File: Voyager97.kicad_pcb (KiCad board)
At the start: 2 copper layers, 388.9 x 122.2 mm, 353 parts, among them J1 AVR-ISP-6, Q1 DSS60601MZ4-13, SW1 SW_Push, U1 AT90USB1286-AU, U2 PRTR5V0U2X, Y1 16MHz

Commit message: Generate production data
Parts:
- added G***: LOGO, locallib:ai-ring-6mm-FancyAss, B.Cu at (139.7, 136.5)
- added G***: LOGO, locallib:ai-ring-6mm-FancyAss-Mask, B.Cu at (139.7, 136.5)
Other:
- board text added: "Designed by ai03"

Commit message: Routing tweaks
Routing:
- net LEDGND: track 2355.3 -> 2356.9 mm
- net ROW3: track 473.7 -> 472.5 mm

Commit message: Add flex cut in center
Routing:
- net COL6: track 289.6 -> 483.0 mm
- net COL7: track 270.4 -> 447.7 mm
- net COL5: track 331.5 -> 488.2 mm
- net COL8: track 252.2 -> 392.7 mm
- net COL4: track 328.9 -> 448.7 mm
- net COL9: track 266.4 -> 370.1 mm
- net COL3: track 350.0 -> 428.4 mm, vias 0 -> 1
- net COL10: track 240.4 -> 304.7 mm, vias 0 -> 1
- net COL2: track 391.8 -> 433.4 mm, vias 0 -> 1
- net +5V: track 2867.6 -> 2836.5 mm, vias 7 -> 8
- net COL11: track 215.7 -> 244.2 mm, vias 0 -> 1
- net COL1: track 389.1 -> 395.3 mm
- net RESET: track 409.9 -> 408.0 mm
- net COL12: track 202.8 -> 203.8 mm
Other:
- outline, holes or cut-outs redrawn

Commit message: Add more flex cutouts
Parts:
- removed SW1: SW_Push, Molex-0548190589:PushButton_6x6mm_TH
- moved D52 20.6 mm to (56.4, 100.0)
- moved R52 20.6 mm to (56.4, 105.6)
- moved D47 15.9 mm to (271.5, 81.0)
- moved D63 15.9 mm to (257.2, 100.0)
- moved R47 15.9 mm to (271.5, 86.5)
- moved R63 15.9 mm to (257.2, 105.6)
- moved D77 15.9 mm to (247.7, 119.1)
- moved R77 15.9 mm to (247.7, 124.6)
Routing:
- net RESET: track 408.0 -> 46.1 mm, vias 3 -> 0
- net GND: track 546.9 -> 201.5 mm, vias 4 -> 3
- net ROW3: track 472.5 -> 455.6 mm
- net LEDGND: track 2356.9 -> 2346.1 mm
- net Net-(D63-Pad2): track 6.62 -> 16.2 mm, vias 0 -> 1
- net Net-(D47-Pad2): track 6.62 -> 12.7 mm
- net Net-(D77-Pad2): track 6.62 -> 12.7 mm
- net ROW4: track 424.0 -> 428.8 mm
- net ROW2: track 393.3 -> 398.1 mm
- net Net-(MX_'1-Pad4): track 7.18 -> 10.9 mm
- net COL11: track 244.2 -> 247.3 mm
- net Net-(MX_]1-Pad4): track 7.18 -> 10.0 mm
- net Net-(MX_/1-Pad4): track 7.18 -> 10.0 mm
- net Net-(CL1-1-Pad2): track 16.4 -> 18.5 mm
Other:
- outline, holes or cut-outs redrawn

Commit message: Adjust cutout location for durability
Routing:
- net LEDGND: track 2346.1 -> 2344.7 mm
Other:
- outline, holes or cut-outs redrawn

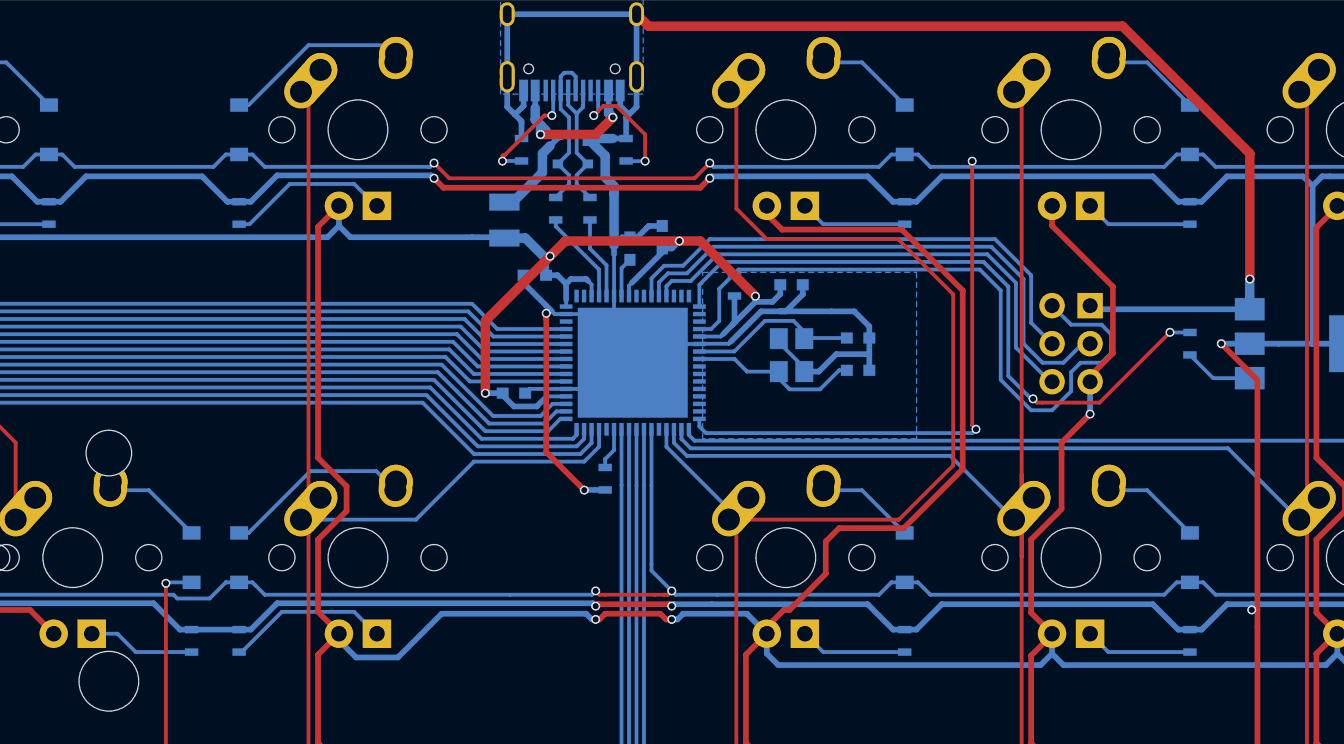
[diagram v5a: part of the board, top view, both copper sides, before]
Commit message: Optimizations
- Crystal placement
- Tracks near SPI header
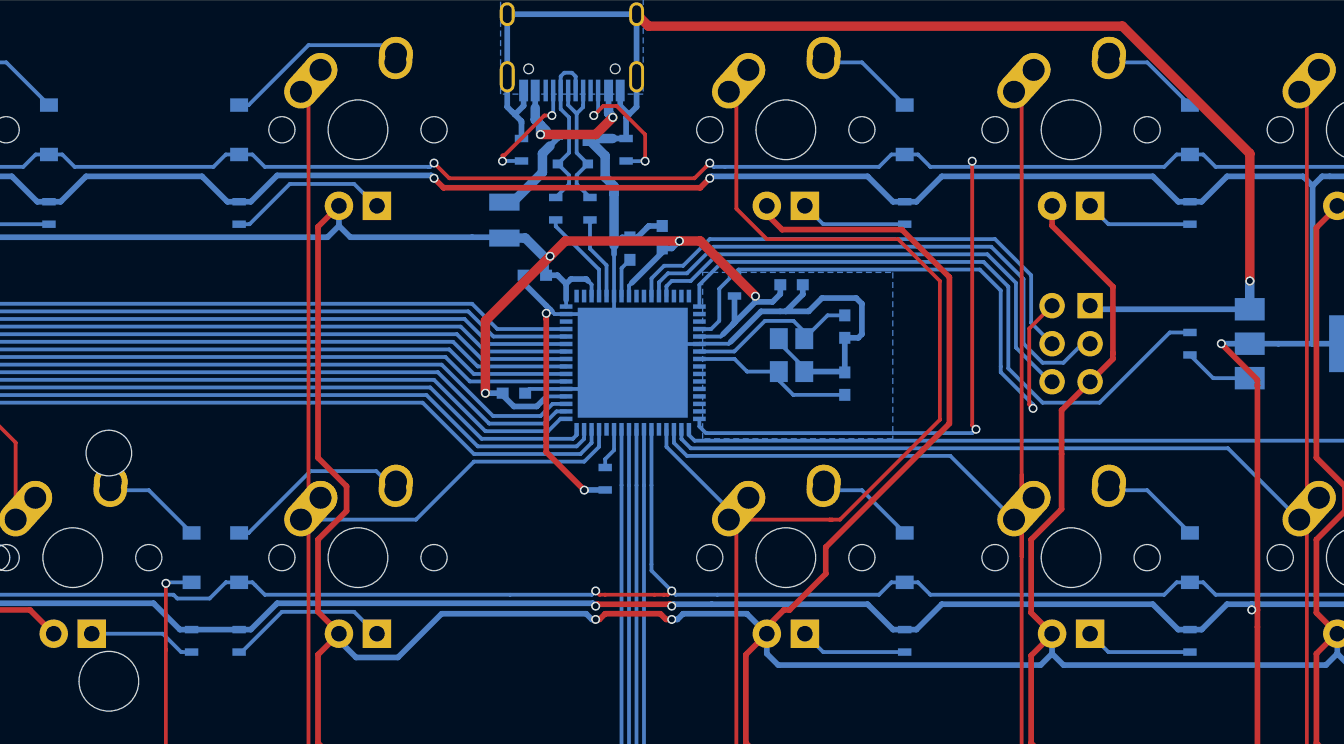
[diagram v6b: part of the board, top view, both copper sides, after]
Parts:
- moved C3 1.26 mm to (359.5, 50.3), turned to 90 degrees
- moved C4 1.17 mm to (359.5, 46.5), turned to 270 degrees
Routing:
- net RESET: track 46.1 -> 40.0 mm, vias 0 -> 1
- net +5V: track 2836.5 -> 2833.3 mm, vias 8 -> 7
- net COL15: track 149.9 -> 147.0 mm
- net Net-(RC5-Pad1): track 44.2 -> 43.9 mm, vias 2 -> 0
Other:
- net class Power: trace_width 0.381 -> 0.635

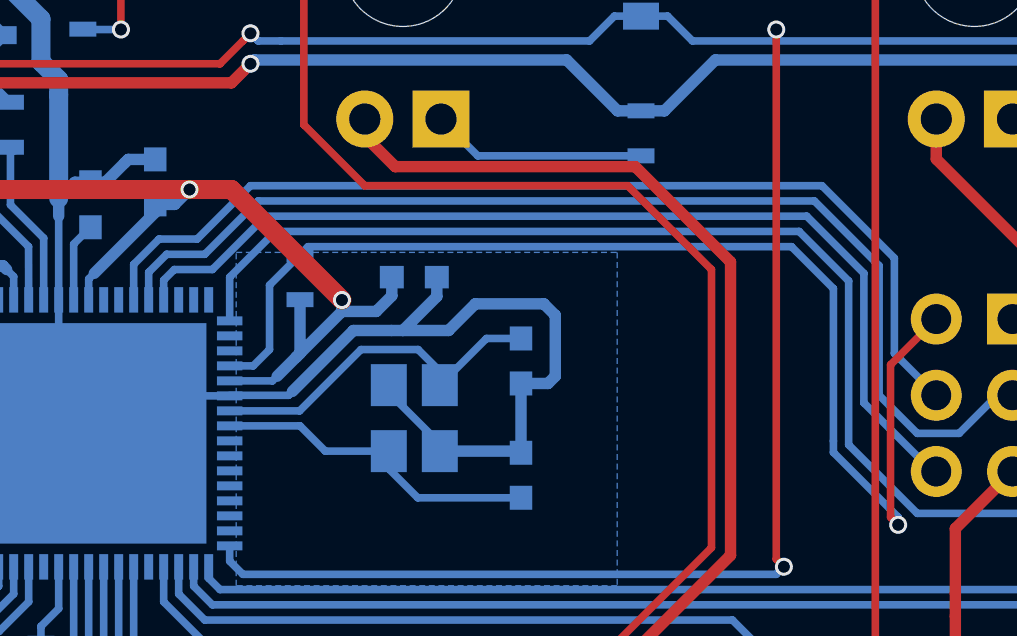
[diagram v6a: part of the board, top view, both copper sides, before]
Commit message: Reposition decoupling capacitor for greater effectiveness
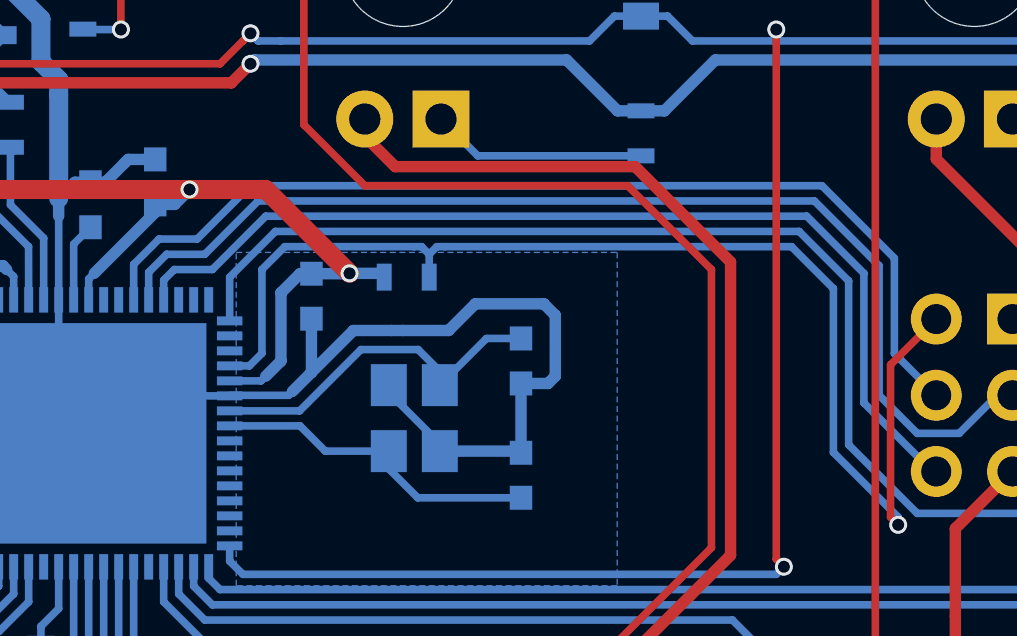
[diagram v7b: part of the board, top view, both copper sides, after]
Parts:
- moved RC3 3.56 mm to (355.7, 43.7), turned to 0 degrees
- moved C8 3.49 mm to (352.6, 44.3), turned to 90 degrees
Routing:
- net +5V: track 2833.3 -> 2831.6 mm
- net RESET: track 40.0 -> 41.3 mm
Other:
- net class Power: trace_width 0.635 -> 0.381

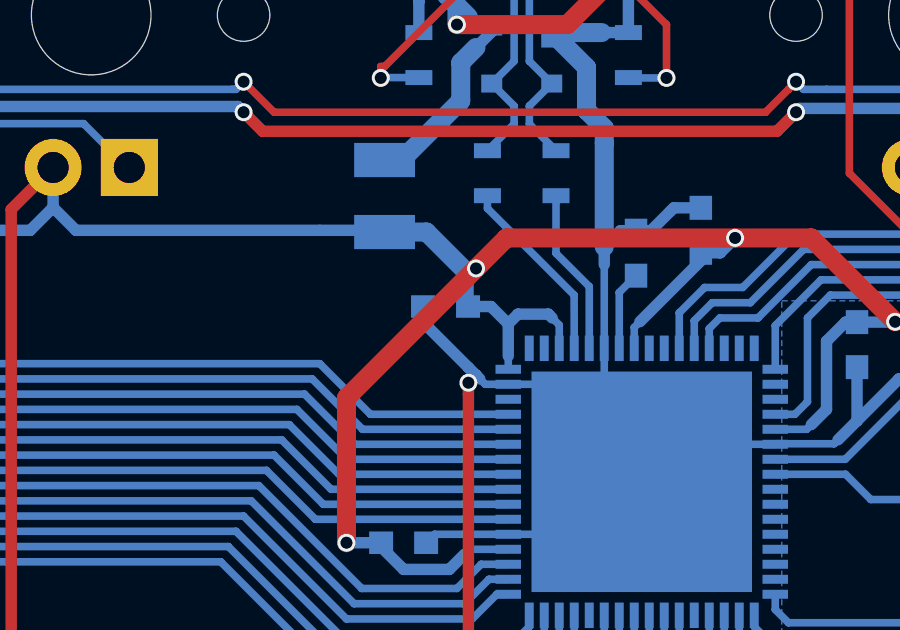
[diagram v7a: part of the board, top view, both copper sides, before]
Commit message: Locallib doesn't even contain amtra's footprints anymore
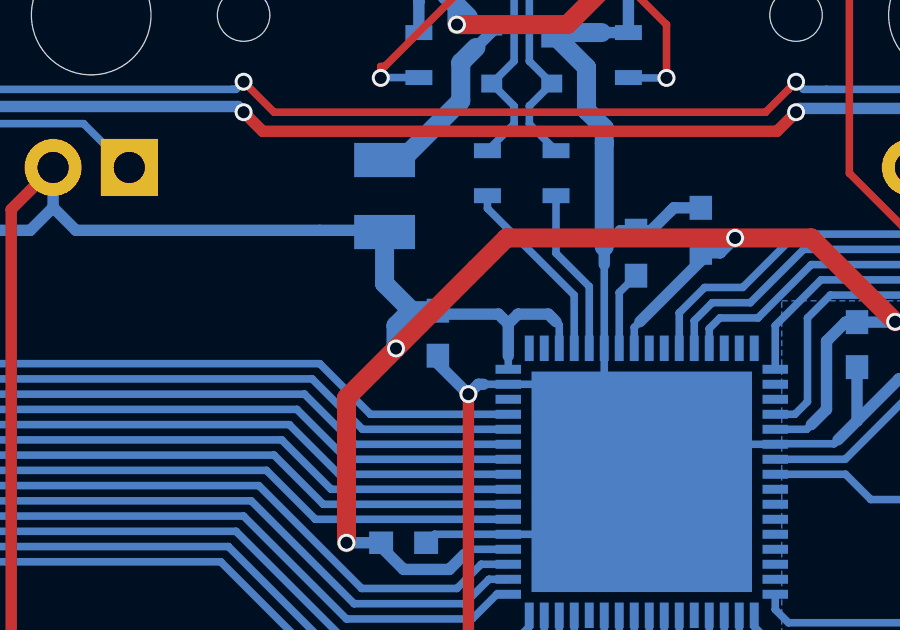
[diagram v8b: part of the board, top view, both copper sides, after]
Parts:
- moved C5 0.92 mm to (338.6, 43.9), turned to 90 degrees
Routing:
- net GND: track 200.8 -> 199.0 mm
- net +5V: track 2831.6 -> 2833.1 mm
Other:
- net class Power: trace_width 0.381 -> 0.635
